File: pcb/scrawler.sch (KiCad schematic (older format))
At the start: 23 parts

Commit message: started design, made components list
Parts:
- removed C?: 1uF, symbol Device:C_Small
- removed C? (x3): 0.1uF, symbol Device:C_Small
- removed C?: 10uF, symbol Device:C_Small
- removed C? (x2): 22pF, symbol Device:C_Small
- removed D? (x3): D_Small, symbol Device:D_Small
- removed F?: 500mA, symbol Device:Polyfuse_Small
- removed MX? (x3): MX-NoLED, symbol MX_Alps_Hybrid:MX-NoLED
- removed R? (x2): 10k, symbol Device:R_Small
- removed R? (x2): 22, symbol Device:R_Small
- removed SW?: SW_Push, symbol Switch:SW_Push
- removed U?: ATmega32U4-AU, Package_QFP:TQFP-44_10x10mm_P0.8mm, symbol MCU_Microchip_ATmega:ATmega32U4-AU
- removed U?: USB-Mini, symbol keebio:USB-Mini
- removed U?: TRRS, symbol keebio:TRRS
- removed Y?: 16MHz, symbol Device:Crystal_GND24_Small
- added D?: D_Small, symbol Device:D_Small
- added SW1, SW10, SW11, SW12, SW13, SW14, SW15, SW16, SW17, SW18, SW19, SW2, SW20, SW21, SW22, SW23, SW3, SW4, SW5, SW6, SW7, SW8, SW9: switch, symbol Switch:SW_Push
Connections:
- net labels removed: +5V, D+, D-, GND, VCC
- wire segments 46 -> 0

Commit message: laptop commit
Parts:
- added D10, D11, D12, D13, D14, D15, D16, D17, D18, D19, D2, D20, D21, D22, D23, D3, D4, D5, D6, D7, D8, D9: diode, symbol Device:D_Small
- D1: renamed from D?; value D_Small -> diode
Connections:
- net COL0: now reaches SW1.2
- net COL0: now also SW12.2, SW18.2, SW21.2, SW6.2
- net at SW2.1: now also D2.2 (A)
- net COL1: now reaches SW2.2
- net COL1: now also SW13.2, SW19.2, SW22.2, SW7.2
- net at SW3.1: now also D3.2 (A)
- net COL2: now reaches SW3.2
- net COL2: now also SW14.2, SW20.2, SW23.2, SW8.2
- net at SW4.1: now also D4.2 (A)
- net COL3: now reaches SW4.2
- net COL3: now also SW15.2, SW9.2
- net at SW5.1: now also D5.2 (A)
- net COL4: now reaches SW5.2
- net COL4: now also SW10.2, SW16.2
- net at SW6.1: now also D6.2 (A)
- net at SW7.1: now also D7.2 (A)
- net at SW8.1: now also D8.2 (A)
- net at SW9.1: now also D9.2 (A)
- net at SW10.1: now also D10.2 (A)
- net at SW12.1: now also D12.2 (A)
- net at SW13.1: now also D13.2 (A)
- net at SW14.1: now also D14.2 (A)
- net at SW15.1: now also D15.2 (A)
- net at SW16.1: now also D16.2 (A)
- net at SW11.1: now also D11.2 (A)
- net COL5: now reaches SW11.2
- net COL5: now also SW17.2
- net at SW17.1: now also D17.2 (A)
- net at SW18.1: now also D18.2 (A)
- net at SW19.1: now also D19.2 (A)
- net at SW20.1: now also D20.2 (A)
- net at SW21.1: now also D21.2 (A)
- net at SW22.1: now also D22.2 (A)
- net at SW23.1: now also D23.2 (A)
- net ROW0: now reaches D1.1 (K)
- net ROW0: now also D2.1 (K), D3.1 (K), D4.1 (K), D5.1 (K)
- new net ROW1: D10.1 (K), D11.1 (K), D6.1 (K), D7.1 (K), D8.1 (K), D9.1 (K)
- new net ROW2: D12.1 (K), D13.1 (K), D14.1 (K), D15.1 (K), D16.1 (K), D17.1 (K)
- new net ROW3: D18.1 (K), D19.1 (K), D20.1 (K)
- new net ROW4: D21.1 (K), D22.1 (K), D23.1 (K)

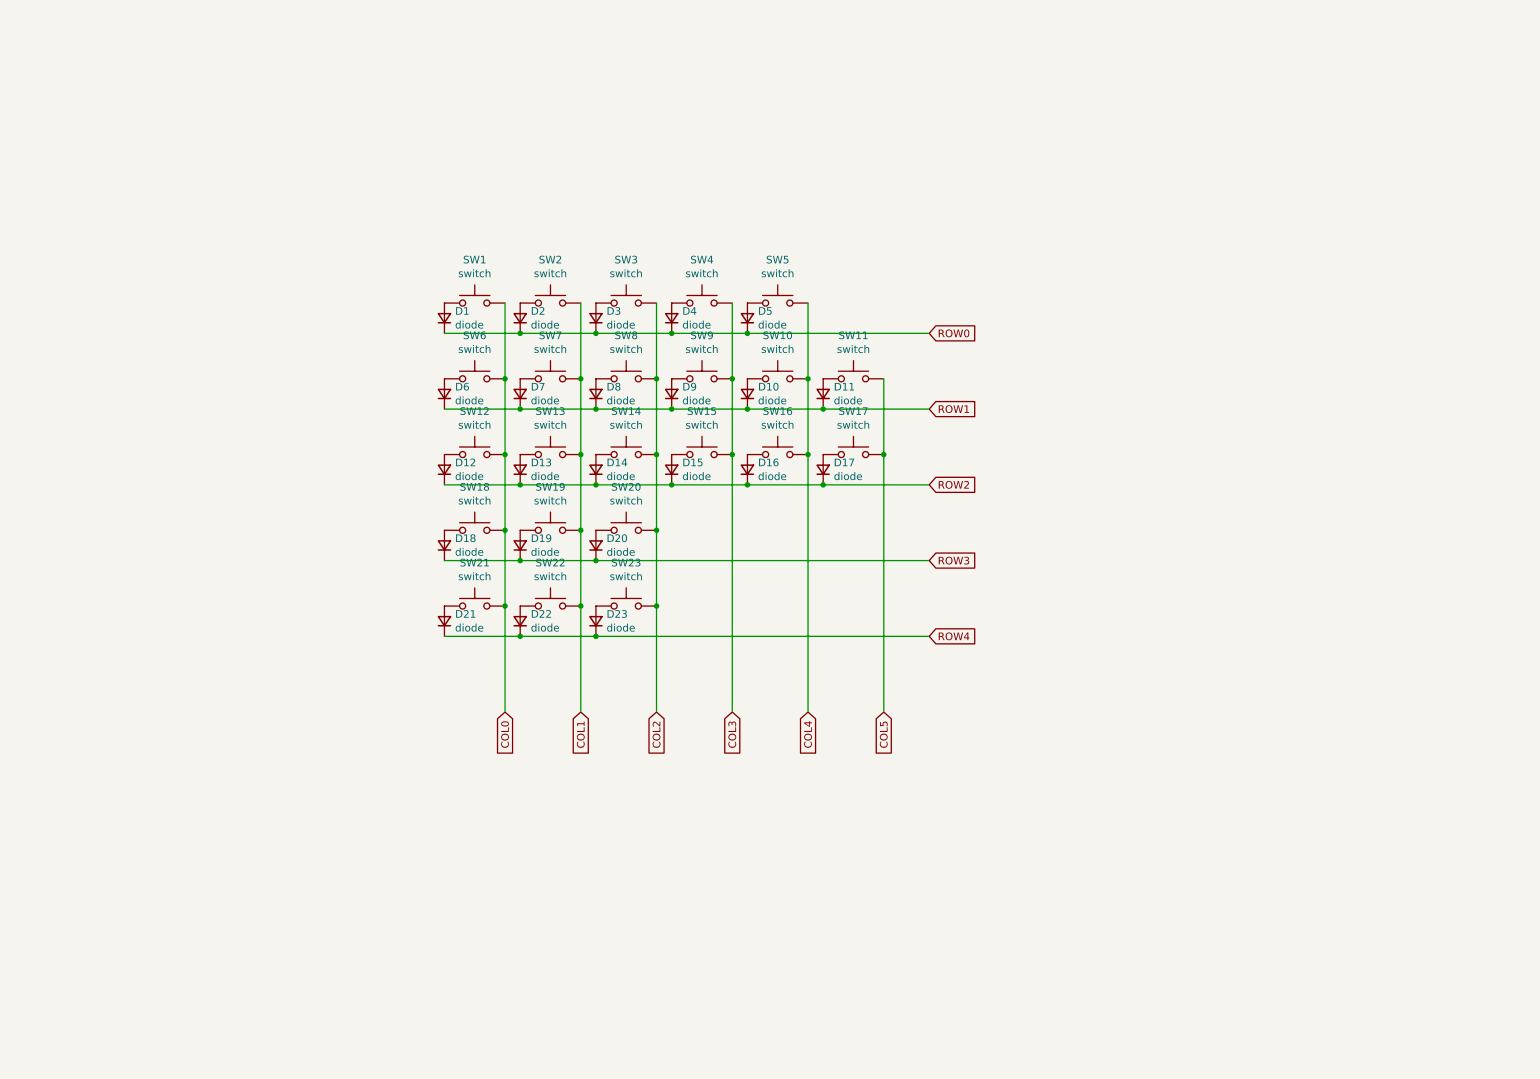
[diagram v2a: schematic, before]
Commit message: decided no resistors/switch for now
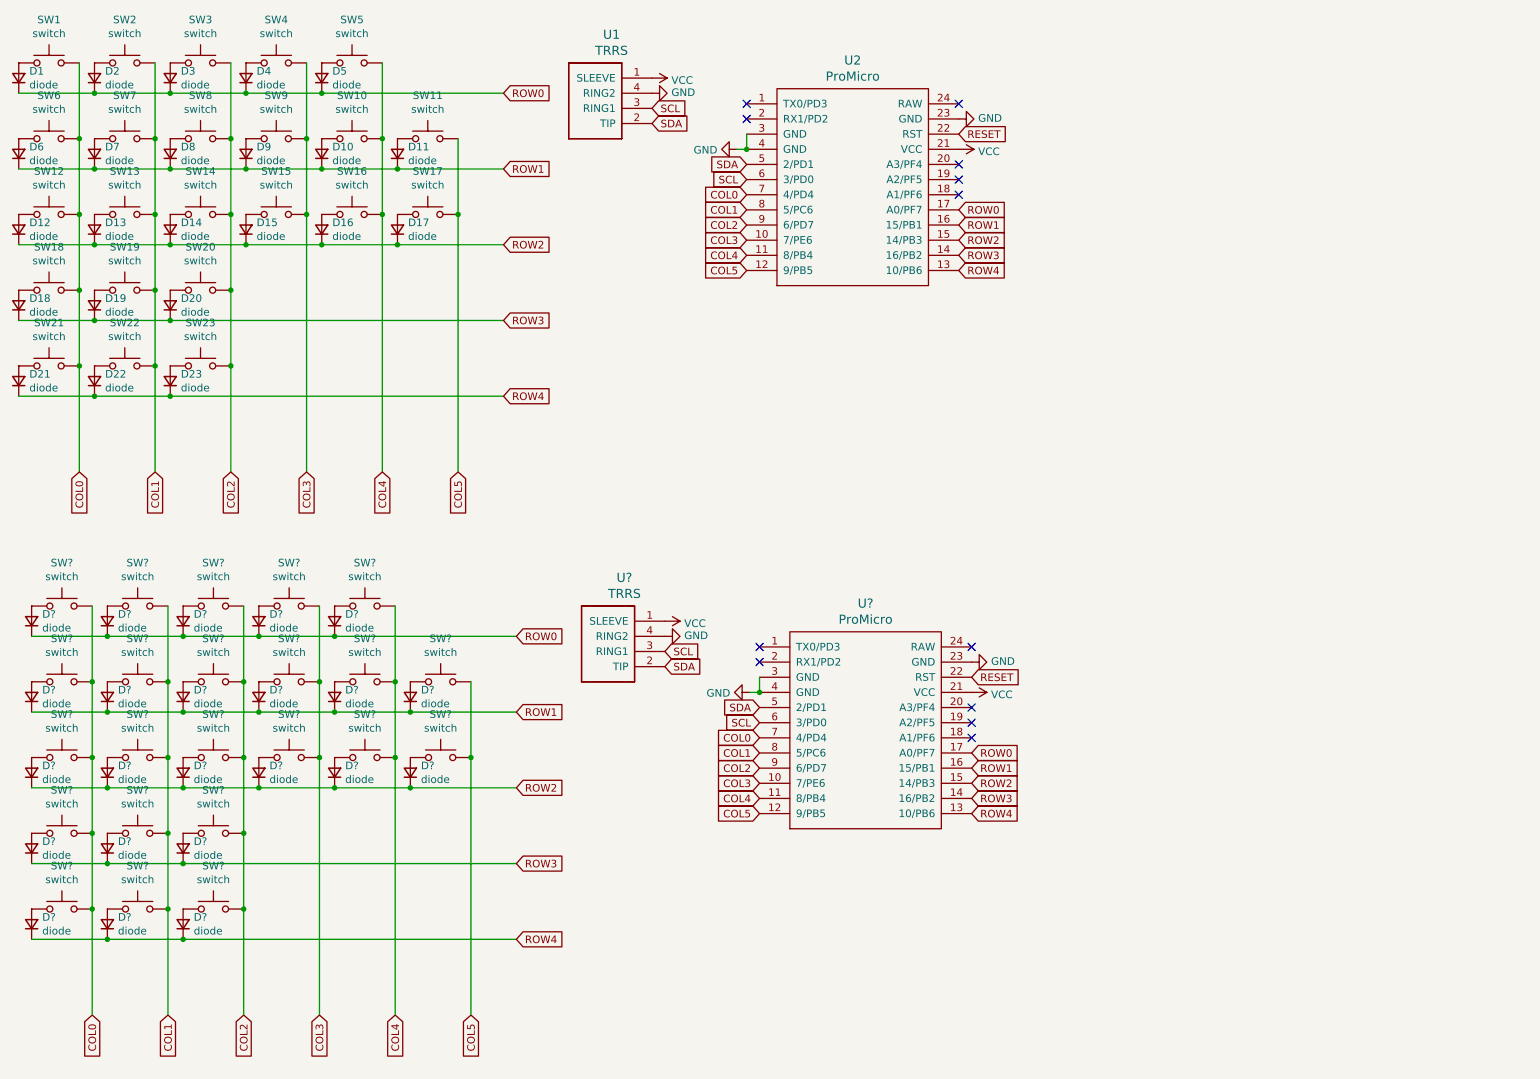
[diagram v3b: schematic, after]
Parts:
- added D? (x23): diode, symbol Device:D_Small
- added SW? (x23): switch, symbol Switch:SW_Push
- added U1, U?: TRRS, symbol keebio:TRRS
- added U2, U?: ProMicro, symbol keebio:ProMicro
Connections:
- net COL0: now also SW?.2, SW?.2, SW?.2, SW?.2, SW?.2, U2.7 (4/PD4), U?.7 (4/PD4)
- net COL1: now also SW?.2, SW?.2, SW?.2, SW?.2, SW?.2, U2.8 (5/PC6), U?.8 (5/PC6)
- net COL2: now also SW?.2, SW?.2, SW?.2, SW?.2, SW?.2, U2.9 (6/PD7), U?.9 (6/PD7)
- net COL3: now also SW?.2, SW?.2, SW?.2, U2.10 (7/PE6), U?.10 (7/PE6)
- net COL4: now also SW?.2, SW?.2, SW?.2, U2.11 (8/PB4), U?.11 (8/PB4)
- net COL5: now also SW?.2, SW?.2, U2.12 (9/PB5), U?.12 (9/PB5)
- net ROW0: now also D?.1 (K), D?.1 (K), D?.1 (K), D?.1 (K), D?.1 (K), U2.17 (A0/PF7), U?.17 (A0/PF7)
- net ROW1: now also D?.1 (K), D?.1 (K), D?.1 (K), D?.1 (K), D?.1 (K), D?.1 (K), U2.16 (15/PB1), U?.16 (15/PB1)
- net ROW2: now also D?.1 (K), D?.1 (K), D?.1 (K), D?.1 (K), D?.1 (K), D?.1 (K), U2.15 (14/PB3), U?.15 (14/PB3)
- net ROW3: now also D?.1 (K), D?.1 (K), D?.1 (K), U2.14 (16/PB2), U?.14 (16/PB2)
- net ROW4: now also D?.1 (K), D?.1 (K), D?.1 (K), U2.13 (10/PB6), U?.13 (10/PB6)
- new net: D?.2 (A), SW?.1 (x23)
- new net GND: U1.4 (RING2), U2.23 (GND), U2.3 (GND), U2.4 (GND), U?.23 (GND), U?.3 (GND), U?.4 (GND), U?.4 (RING2)
- new net RESET: U2.22 (RST), U?.22 (RST)
- new net SCL: U1.3 (RING1), U2.6 (3/PD0), U?.3 (RING1), U?.6 (3/PD0)
- new net SDA: U1.2 (TIP), U2.5 (2/PD1), U?.2 (TIP), U?.5 (2/PD1)
- new net VCC: U1.1 (SLEEVE), U2.21 (VCC), U?.1 (SLEEVE), U?.21 (VCC)
- no-connect marks 0 -> 12
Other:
- moved on the sheet: D1, D10, D11, D12, D13, D14, D15, D16, D17, D18, D19, D2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

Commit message: started physical pcb
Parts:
- removed D? (x23): diode, symbol Device:D_Small
- removed SW? (x23): switch, symbol Switch:SW_Push
- removed U?: TRRS, symbol keebio:TRRS
- removed U?: ProMicro, symbol keebio:ProMicro
- added H1, H2, H3, H4, H5, H6: Hole, Keebio-Parts:MountingHole, symbol keebio:Hole
- D1, D10, D11, D12, D13, D14, D15, D16, D17, D18, D19, D2, D20, D21, D22, D23, D3, D4, D5, D6, D7, D8, D9: footprint (none) -> Keebio-Parts:Diode
- SW1, SW10, SW11, SW12, SW13, SW14, SW15, SW16, SW17, SW18, SW19, SW2, SW20, SW21, SW22, SW23, SW3, SW4, SW5, SW6, SW7, SW8, SW9: footprint (none) -> keyswitches:Kailh_socket_PG1350_reversible
- U1: footprint (none) -> Keebio-Parts:TRRS-PJ-320A-dual
- U2: footprint (none) -> Keebio-Parts:ArduinoProMicro
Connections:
- no-connect marks 12 -> 3
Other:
- moved on the sheet: D1, D10, D11, D12, D13, D14, D15, D16, D17, D18, D19, D2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

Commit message: clean root dir
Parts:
- added R1, R2: R, Keebio-Parts:Resistor, symbol Device:R
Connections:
- net GND: now also U1.3 (RING1); no longer U1.4 (RING2)
- net ROW0: now also U2.13 (10/PB6); no longer U2.17 (A0/PF7)
- net ROW1: now also U2.14 (16/PB2); no longer U2.16 (15/PB1)
- net ROW3: now also U2.16 (15/PB1); no longer U2.14 (16/PB2)
- net ROW4: now also U2.17 (A0/PF7); no longer U2.13 (10/PB6)
- net SCL: now also U1.1 (SLEEVE), R2.2; no longer U1.3 (RING1)
- net SDA: now also R1.2
- net VCC: now also U1.4 (RING2), R1.1, R2.1; no longer U1.1 (SLEEVE)
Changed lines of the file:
@@
 L keebio:TRRS U1
 U 1 1 60A4975E
-P 8075 4690
-F 0 "U1" H 7992 4503 60  0000 C CNN
-F 1 "TRRS" H 7992 4609 60  0000 C CNN
-F 2 "Keebio-Parts:TRRS-PJ-320A-dual" H 8225 4690 60  0001 C CNN
-F 3 "" H 8225 4690 60  0001 C CNN
-	1    8075 4690
+P 8080 4700
+F 0 "U1" H 7997 4513 60  0000 C CNN
+F 1 "TRRS" H 7997 4619 60  0000 C CNN
+F 2 "Keebio-Parts:TRRS-PJ-320A-dual" H 8230 4700 60  0001 C CNN
+F 3 "" H 8230 4700 60  0001 C CNN
+	1    8080 4700
 	1    0    0    -1
 $EndComp
@@
 Text GLabel 6655 3630 0    50   Input ~ 0
 COL5
-Text GLabel 8055 3230 2    50   Input ~ 0
+Text GLabel 8055 3630 2    50   Input ~ 0
 ROW0
-Text GLabel 8055 3330 2    50   Input ~ 0
+Text GLabel 8055 3530 2    50   Input ~ 0
 ROW1
 Text GLabel 8055 3430 2    50   Input ~ 0
 ROW2
-Text GLabel 8055 3530 2    50   Input ~ 0
+Text GLabel 8055 3330 2    50   Input ~ 0
 ROW3
-Text GLabel 8055 3630 2    50   Input ~ 0
+Text GLabel 8055 3230 2    50   Input ~ 0
 ROW4
 Text GLabel 8055 2730 2    50   Input ~ 0
@@
 L power:VCC #PWR0104
 U 1 1 60A698CA
-P 7725 4590
-F 0 "#PWR0104" H 7725 4440 50  0001 C CNN
-F 1 "VCC" V 7740 4718 50  0000 L CNN
-F 2 "" H 7725 4590 50  0001 C CNN
-F 3 "" H 7725 4590 50  0001 C CNN
-	1    7725 4590
+P 7730 4500
+F 0 "#PWR0104" H 7730 4350 50  0001 C CNN
+F 1 "VCC" V 7745 4628 50  0000 L CNN
+F 2 "" H 7730 4500 50  0001 C CNN
+F 3 "" H 7730 4500 50  0001 C CNN
+	1    7730 4500
 	0    -1   -1   0
 $EndComp
@@
 L power:GND #PWR0105
 U 1 1 60A6A41D
-P 7725 4490
-F 0 "#PWR0105" H 7725 4240 50  0001 C CNN
-F 1 "GND" V 7730 4362 50  0000 R CNN
-F 2 "" H 7725 4490 50  0001 C CNN
-F 3 "" H 7725 4490 50  0001 C CNN
-	1    7725 4490
+P 7730 4400
+F 0 "#PWR0105" H 7730 4150 50  0001 C CNN
+F 1 "GND" V 7735 4272 50  0000 R CNN
+F 2 "" H 7730 4400 50  0001 C CNN
+F 3 "" H 7730 4400 50  0001 C CNN
+	1    7730 4400
 	0    1    1    0
 $EndComp
-Text GLabel 7725 4290 0    50   Input ~ 0
+Text GLabel 7730 4300 0    50   Input ~ 0
 SDA
-Text GLabel 7725 4390 0    50   Input ~ 0
+Text GLabel 7730 4600 0    50   Input ~ 0
 SCL
 $Comp
@@
 	1    0    0    -1
 $EndComp
+$Comp
+L Device:R R1
+U 1 1 60C01C38
+P 6230 1735
+F 0 "R1" H 6300 1781 50  0000 L CNN
+F 1 "R" H 6300 1690 50  0000 L CNN
+F 2 "Keebio-Parts:Resistor" V 6160 1735 50  0001 C CNN
+F 3 "~" H 6230 1735 50  0001 C CNN
+	1    6230 1735
+	1    0    0    -1
+$EndComp
+$Comp
+L Device:R R2
+U 1 1 60C0241A
+P 6540 1740
+F 0 "R2" H 6610 1786 50  0000 L CNN
+F 1 "R" H 6610 1695 50  0000 L CNN
+F 2 "Keebio-Parts:Resistor" V 6470 1740 50  0001 C CNN
+F 3 "~" H 6540 1740 50  0001 C CNN
+	1    6540 1740
+	1    0    0    -1
+$EndComp
+$Comp
+L power:VCC #PWR0106
+U 1 1 60C03FE0
+P 6230 1585
+F 0 "#PWR0106" H 6230 1435 50  0001 C CNN
+F 1 "VCC" H 6245 1758 50  0000 C CNN
+F 2 "" H 6230 1585 50  0001 C CNN
+F 3 "" H 6230 1585 50  0001 C CNN
+	1    6230 1585
+	1    0    0    -1
+$EndComp
+$Comp
+L power:VCC #PWR0107
+U 1 1 60C047F7
+P 6540 1590
+F 0 "#PWR0107" H 6540 1440 50  0001 C CNN
+F 1 "VCC" H 6555 1763 50  0000 C CNN
+F 2 "" H 6540 1590 50  0001 C CNN
+F 3 "" H 6540 1590 50  0001 C CNN
+	1    6540 1590
+	1    0    0    -1
+$EndComp
+Text GLabel 6230 1885 3    50   Input ~ 0
+SDA
+Text GLabel 6540 1890 3    50   Input ~ 0
+SCL
+$Comp
+L power:PWR_FLAG #FLG0101
+U 1 1 60C068F4
+P 5165 1355
+F 0 "#FLG0101" H 5165 1430 50  0001 C CNN
+F 1 "PWR_FLAG" H 5165 1528 50  0000 C CNN
+F 2 "" H 5165 1355 50  0001 C CNN
+F 3 "~" H 5165 1355 50  0001 C CNN
+	1    5165 1355
+	1    0    0    -1
+$EndComp
+$Comp
+L power:GND #PWR0108
+U 1 1 60C073E6
+P 5165 1355
+F 0 "#PWR0108" H 5165 1105 50  0001 C CNN
+F 1 "GND" H 5170 1182 50  0000 C CNN
+F 2 "" H 5165 1355 50  0001 C CNN
+F 3 "" H 5165 1355 50  0001 C CNN
+	1    5165 1355
+	1    0    0    -1
+$EndComp
+$Comp
+L power:PWR_FLAG #FLG0102
+U 1 1 60C07A4D
+P 5490 1360
+F 0 "#FLG0102" H 5490 1435 50  0001 C CNN
+F 1 "PWR_FLAG" H 5490 1533 50  0000 C CNN
+F 2 "" H 5490 1360 50  0001 C CNN
+F 3 "~" H 5490 1360 50  0001 C CNN
+	1    5490 1360
+	-1   0    0    1
+$EndComp
+$Comp
+L power:VCC #PWR0109
+U 1 1 60C0818C
+P 5490 1360
+F 0 "#PWR0109" H 5490 1210 50  0001 C CNN
+F 1 "VCC" H 5505 1533 50  0000 C CNN
+F 2 "" H 5490 1360 50  0001 C CNN
+F 3 "" H 5490 1360 50  0001 C CNN
+	1    5490 1360
+	1    0    0    -1
+$EndComp
